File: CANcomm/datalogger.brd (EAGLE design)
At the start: 53.3 x 56.8 mm, 44 parts, among them J1 MICRO-SD_CARD_SOCKET, Y1 16MHz, Y2 32.768kHz

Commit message: More work
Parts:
- PROGUSB: value USB_MINI-B_SMT -> (none); device SparkFun-Connectors:USB-MINIB -> SparkFun-Connectors:USB-B-MICRO-SMD
- moved PROGUSB 2.84 mm to (31.8, 3.81)
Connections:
- net GND: now also PROGUSB.SHIELD1, PROGUSB.SHIELD2, PROGUSB.SHIELD3; no longer PROGUSB.S1, PROGUSB.S2, PROGUSB.S3, PROGUSB.S4
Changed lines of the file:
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@@
 <attribute name="VALUE" x="23.4696" y="46.2534" size="1.27" layer="27" ratio="10" rot="R180"/>
 </element>
-<element name="PROGUSB" library="SparkFun-Connectors" library_urn="urn:adsk.eagle:library:513" package="USB-MINIB" package3d_urn="urn:adsk.eagle:package:38244/1" value="USB_MINI-B_SMT" x="33.02" y="6.35" smashed="yes" rot="R90">
-<attribute name="NAME" x="28.321" y="5.08" size="0.6096" layer="25" font="vector" ratio="20" rot="R90"/>
-<attribute name="PROD_ID" value="CONN-08193" x="67.31" y="63.5" size="1.778" layer="27" rot="R90" display="off"/>
-<attribute name="SF_ID" value="PRT-00587" x="33.02" y="6.35" size="1.778" layer="27" rot="R90" display="off"/>
-<attribute name="VALUE" x="37.719" y="5.08" size="0.6096" layer="27" font="vector" ratio="20" rot="R90" align="top-left"/>
+<element name="PROGUSB" library="SparkFun-Connectors" library_urn="urn:adsk.eagle:library:513" package="USB-B-MICRO-SMD" package3d_urn="urn:adsk.eagle:package:38238/1" value="" x="31.75" y="3.81" smashed="yes" rot="R90">
+<attribute name="NAME" x="27.051" y="2.54" size="0.6096" layer="25" font="vector" ratio="20" rot="R90"/>
+<attribute name="PROD_ID" value="CONN-11752" x="66.04" y="60.96" size="1.778" layer="27" rot="R90" display="off"/>
+<attribute name="VALUE" x="36.449" y="2.54" size="0.6096" layer="27" font="vector" ratio="20" rot="R90" align="top-left"/>
 </element>
 <element name="PWR" library="con-molex" library_urn="urn:adsk.eagle:library:165" package="22-23-2021" value="22-23-2021" x="5.08" y="3.81" smashed="yes" rot="R180">
@@
 <contactref element="C6" pad="2"/>
 <contactref element="C7" pad="2"/>
-<contactref element="PROGUSB" pad="S1"/>
-<contactref element="PROGUSB" pad="S2"/>
-<contactref element="PROGUSB" pad="S3"/>
+<contactref element="PROGUSB" pad="SHIELD1"/>
+<contactref element="PROGUSB" pad="SHIELD2"/>
+<contactref element="PROGUSB" pad="SHIELD3"/>
 <contactref element="PROGUSB" pad="GND"/>
 <contactref element="BOOTLOADER" pad="6"/>
@@
 <vertex x="0" y="0"/>
 </polygon>
-<contactref element="PROGUSB" pad="S4"/>
 <via x="16.51" y="17.78" extent="1-16" drill="0.35"/>
 <via x="19.05" y="20.32" extent="1-16" drill="0.35"/>
@@
 <wire x1="31.82270625" y1="7.2444" x2="32.1256" y2="7.2444" width="0.4064" layer="1"/>
 <wire x1="32.1256" y1="7.2444" x2="33.02" y2="6.35" width="0.4064" layer="1"/>
-<wire x1="31.42" y1="8.85" x2="31.42" y2="7.64710625" width="0.4064" layer="1"/>
+<wire x1="31.72" y1="9.075" x2="31.42" y2="7.64710625" width="0.4064" layer="1"/>
 <wire x1="31.42" y1="7.64710625" x2="31.82270625" y2="7.2444" width="0.4064" layer="1"/>
 </signal>
@@
 <wire x1="32.4612" y1="9.144" x2="32.4612" y2="10.668" width="0.1524" layer="1"/>
 <wire x1="32.3088" y1="8.9916" x2="32.4612" y2="9.144" width="0.1524" layer="1"/>
-<wire x1="32.3088" y1="8.9916" x2="32.22" y2="8.85" width="0.1524" layer="1"/>
+<wire x1="32.3088" y1="8.9916" x2="32.37" y2="9.075" width="0.1524" layer="1"/>
 <via x="32.4612" y="10.668" extent="1-16" drill="0.35"/>
 </signal>
@@
 <wire x1="33.0708" y1="8.9916" x2="33.0708" y2="10.2108" width="0.1524" layer="1"/>
 <wire x1="36.2712" y1="11.43" x2="36.41" y2="11.43" width="0.1524" layer="16"/>
-<wire x1="33.0708" y1="8.9916" x2="33.02" y2="8.85" width="0.1524" layer="1"/>
+<wire x1="33.0708" y1="8.9916" x2="33.02" y2="9.075" width="0.1524" layer="1"/>
 <via x="33.528" y="10.668" extent="1-16" drill="0.35"/>
 </signal>

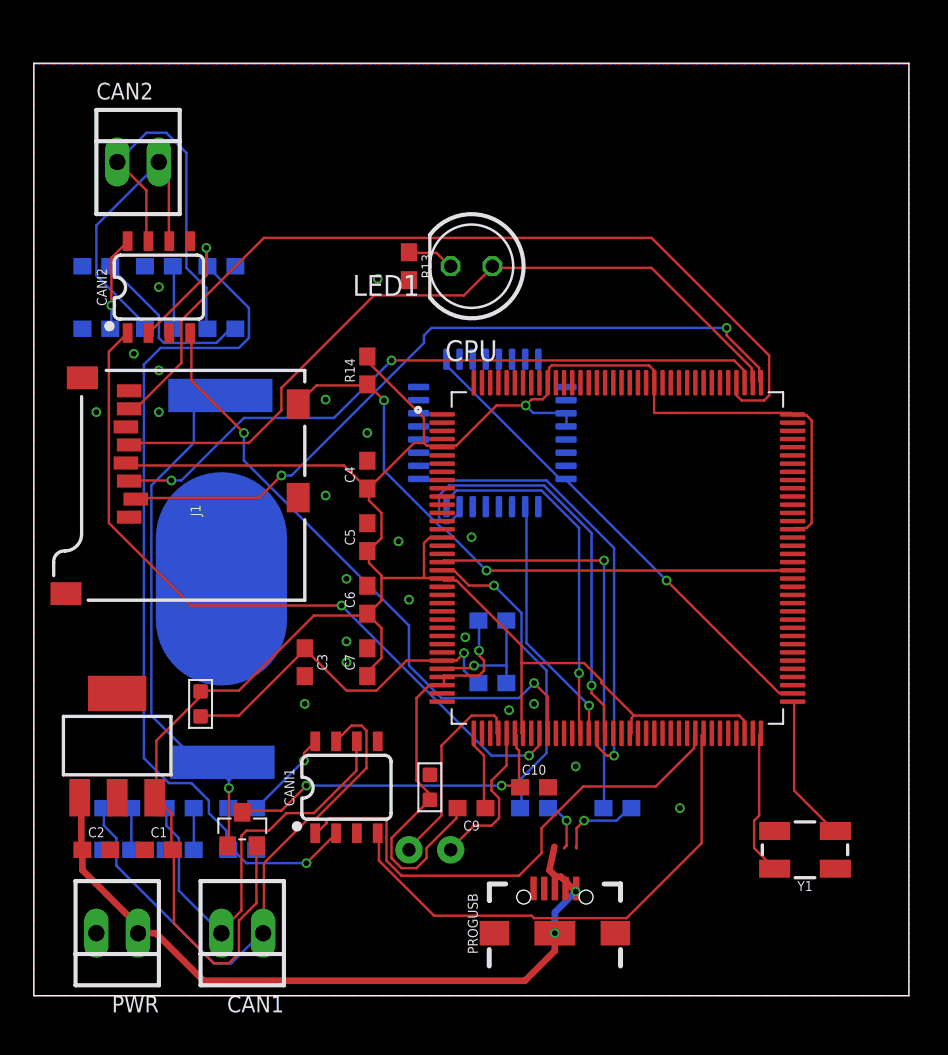
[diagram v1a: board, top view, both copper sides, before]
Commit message: Add USB-C and PRGM button
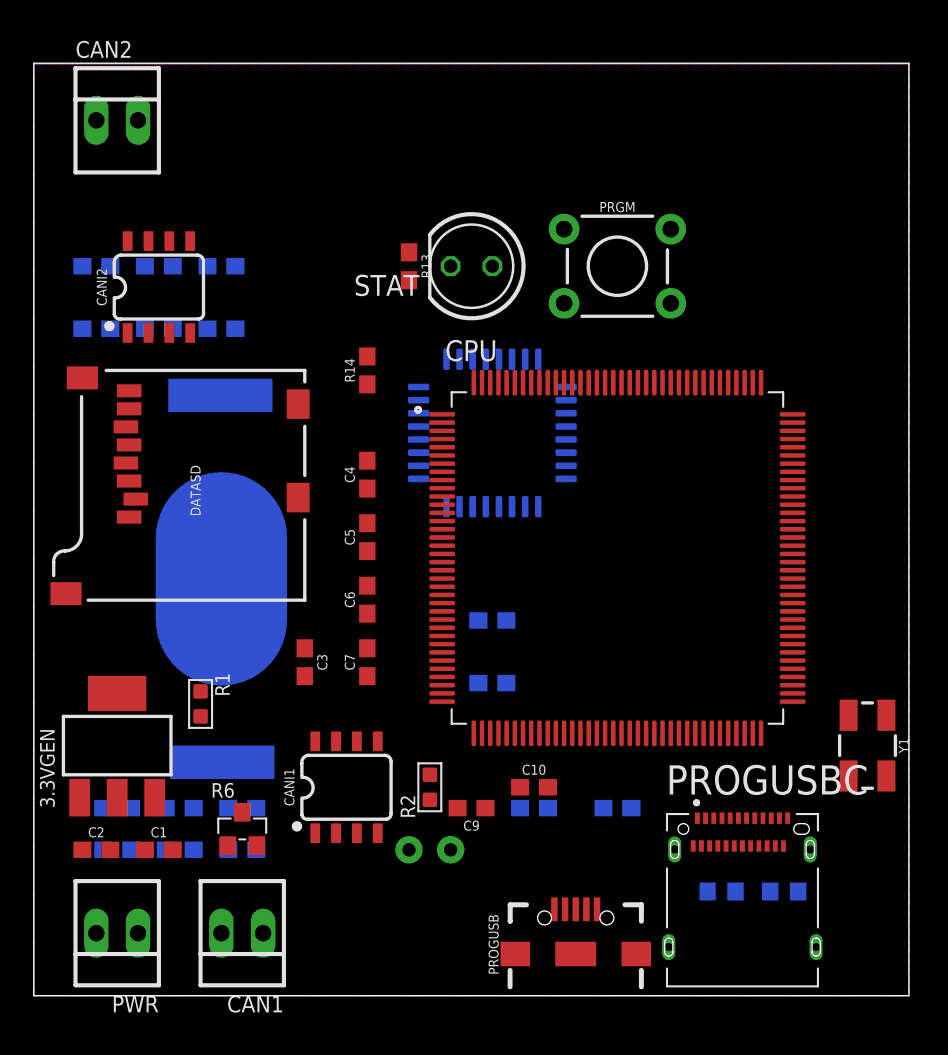
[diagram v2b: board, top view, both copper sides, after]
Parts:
- added PRGM: MOMENTARY-SWITCH-SPST-PTH-6.0MM, SparkFun-Switches:TACTILE_SWITCH_PTH_6.0MM
- added PROGUSBC: 12401610E4#2A, 12401610E4_2A:AMPHENOL_12401610E4#2A
- added R15, R16: 5.1k, rcl:R0603
- moved Y1 7.41 mm to (50.8, 15.2), turned to 270 degrees
- moved CAN2 2.84 mm to (5.08, 53.3)
- moved PROGUSB 1.80 mm to (33.0, 2.54)
- renumbered J1 to DATASD, LED1 to STAT
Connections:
- removed net N$6: PROGUSB.D-, R4.2
- removed net N$7: PROGUSB.D+, R5.2
- new net N$11: PROGUSBC.B5, R16.2
- new net N$9: PROGUSBC.A5, R15.2
- new net USBD+: PROGUSB.D+, PROGUSBC.A6, PROGUSBC.B6, R5.2
- new net USBD-: PROGUSB.D-, PROGUSBC.A7, PROGUSBC.B7, R4.2
- net GND: now also PRGM.1, PROGUSBC.A1, PROGUSBC.A12, PROGUSBC.B1, PROGUSBC.B12, PROGUSBC.S1, PROGUSBC.S2, PROGUSBC.S3, PROGUSBC.S4, R15.1, R16.1
- net PRGM: now also PRGM.3
- net VCC: now also PROGUSBC.A4, PROGUSBC.A9, PROGUSBC.B4, PROGUSBC.B9
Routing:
- net 3.3V: track 157.4 -> 0.00 mm, vias 1 -> 0
- net 5V: track 60.5 -> 0.00 mm, vias 2 -> 0
- net 0MISO: track 53.2 -> 0.00 mm
- net 0SCK: track 46.7 -> 0.00 mm
- net CAN2TX: track 45.1 -> 0.00 mm, vias 2 -> 0
- net VCC: track 44.9 -> 0.00 mm, vias 2 -> 0
- net 0CS0: track 44.8 -> 0.00 mm, vias 2 -> 0
- net 0MOSI: track 41.5 -> 0.00 mm, vias 2 -> 0
- net CAN2RX: track 38.0 -> 0.00 mm, vias 2 -> 0
- net SDCD: track 37.8 -> 0.00 mm, vias 2 -> 0
- net N$10: track 35.9 -> 0.00 mm, vias 1 -> 0
- net CAN1H: track 33.7 -> 0.00 mm
- net CAN1TX: track 31.5 -> 0.00 mm
- net CAN1RX: track 31.4 -> 0.00 mm
- net RESET: track 29.8 -> 0.00 mm, vias 1 -> 0
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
